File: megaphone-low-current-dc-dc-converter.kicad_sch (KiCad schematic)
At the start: 7 parts, among them U2 AP63203WU

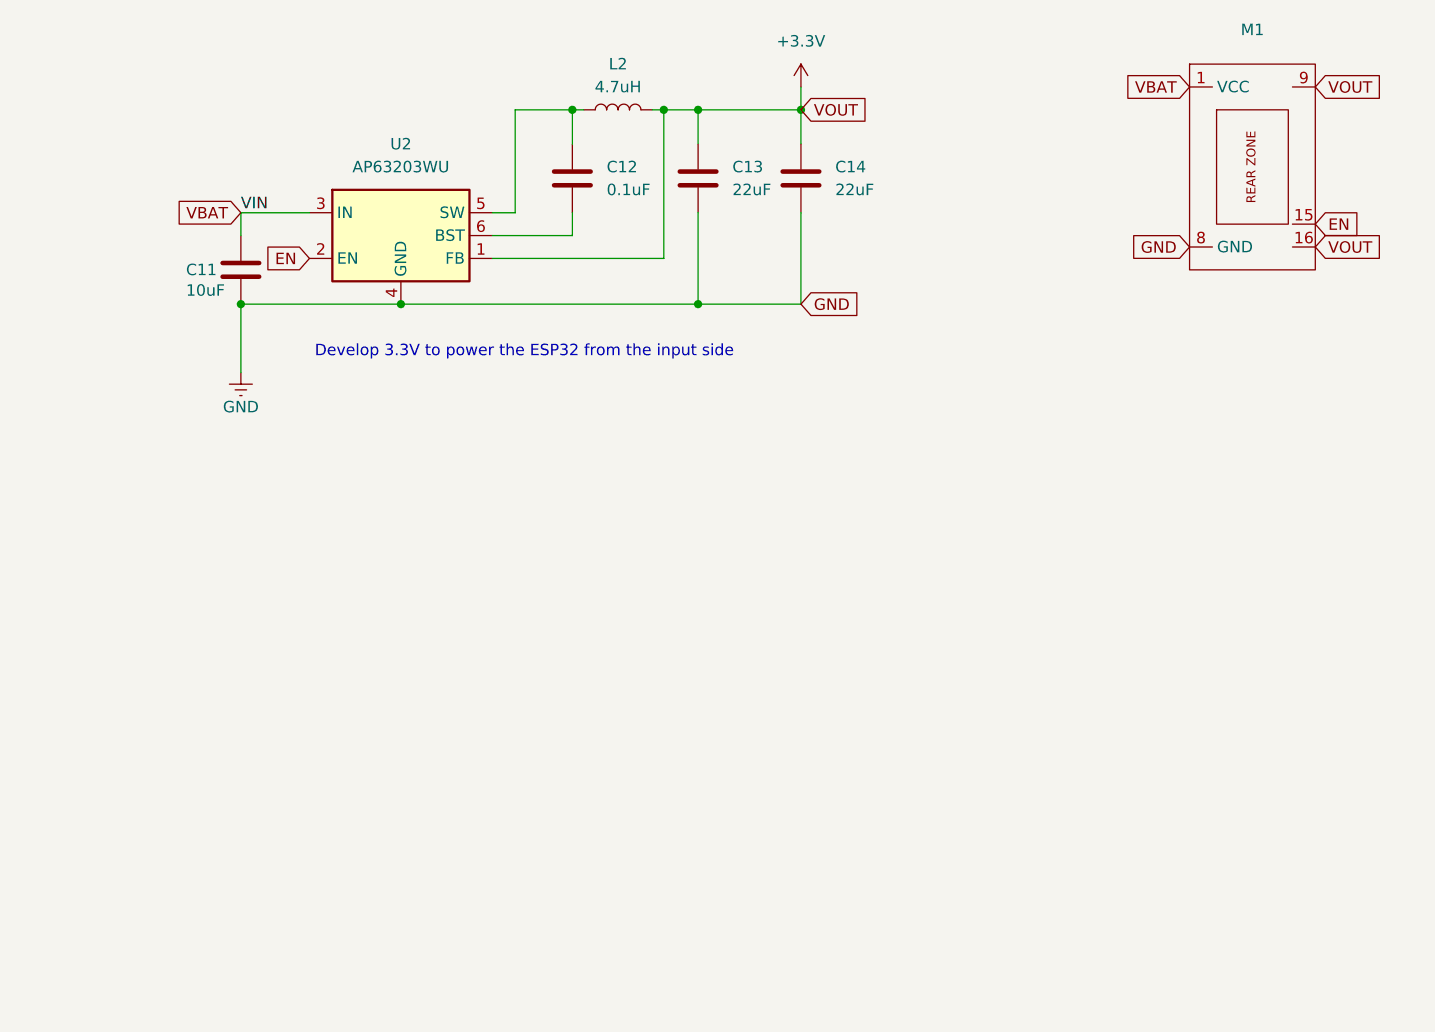
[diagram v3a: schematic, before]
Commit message: use TPS631000 DC:DC converter
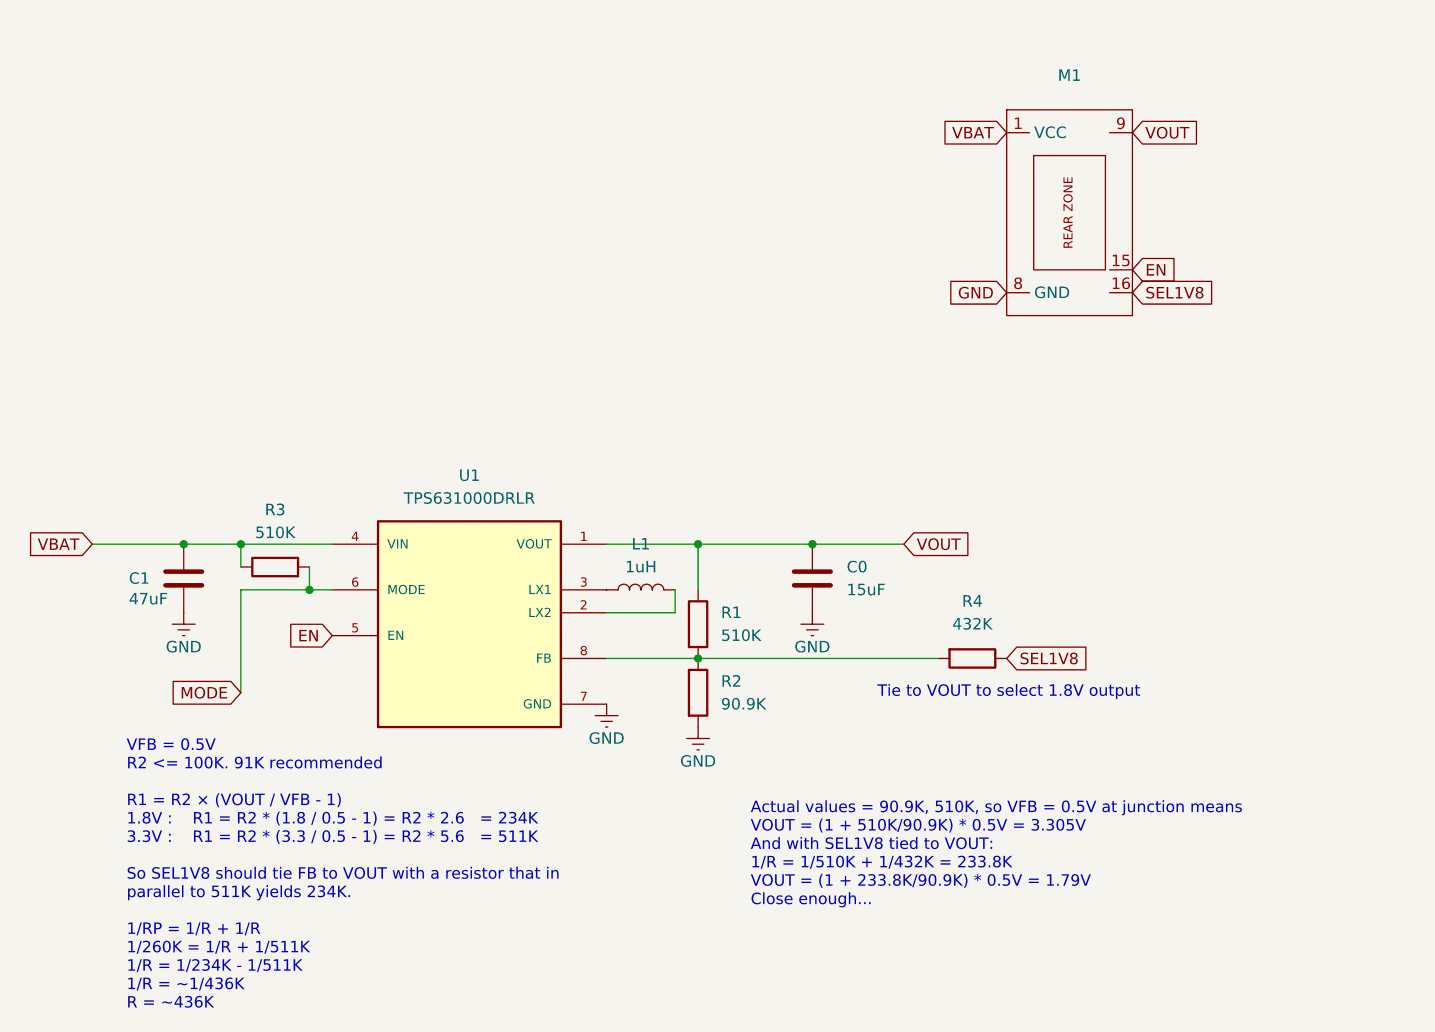
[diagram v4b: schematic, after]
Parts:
- removed C12: 0.1uF, Capacitor_SMD:C_0603_1608Metric, symbol Device:C
- removed C13, C14: 22uF, Capacitor_SMD:C_0603_1608Metric, symbol Device:C
- removed U2: AP63203WU, Package_TO_SOT_SMD:TSOT-23-6, symbol Regulator_Switching:AP63203WU
- added C0: 15uF, Capacitor_SMD:C_0805_2012Metric, symbol Device:C
- added R1, R3: 510K, Resistor_SMD:R_0805_2012Metric, symbol Device:R
- added R2: 90.9K, Resistor_SMD:R_0805_2012Metric, symbol Device:R
- added R4: 432K, Resistor_SMD:R_0805_2012Metric, symbol Device:R
- added U1: TPS631000DRLR, megaphone-low-current-dc-dc-converter:SOT50P160X60-8N, symbol TPS631000DRLR:TPS631000DRLR
- C1: renamed from C11; value 10uF -> 47uF; footprint Capacitor_SMD:C_0603_1608Metric -> Capacitor_SMD:C_0805_2012Metric
- L1: renamed from L2; value 4.7uH -> 1uH; footprint Inductor_SMD:L_Vishay_IFSC-1515AH_4x4x1.8mm -> Inductor_SMD:L_1008_2520Metric_Pad1.43x2.20mm_HandSolder
- M1: footprint MegaCastle:MegaCastle2x8-Module-I7.0x15.5-M8183 -> MegaCastle:MegaCastle2x8-Module-I7.0x15.5-M8183-PANEL-NIBBLE
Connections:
- net EN: now also U1.5 (EN)
- net GND: now also C0.2, R2.2, U1.7 (GND)
- net VBAT: now also R3.1, U1.4 (VIN)
- net at L1.1: now also U1.3 (LX1)
- removed net +3.3V: L1.2, M1.16, M1.9
- new net: R1.2, R2.1, R4.2, U1.8 (FB)
- new net: L1.2, U1.2 (LX2)
- new net MODE: R3.2, U1.6 (MODE)
- new net SEL1V8: M1.16, R4.1
- new net VOUT: C0.1, M1.9, R1.1, U1.1 (VOUT)
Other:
- note added: "Actual values = 90.9K, 510K, so VFB = 0.5V at junction means VOUT = (1 + 510K/90.9K) * 0.5V = 3.305V And with SEL1V8 tied to VOUT: 1/R = 1/510K + 1/432K = 233.8K VOUT = (1 + 233.8K/90.9K) * 0.5V = 1.79V Close enough..."
- note added: "Tie to VOUT to select 1.8V output"
- note added: "VFB = 0.5V R2 <= 100K. 91K recommended R1 = R2 × (VOUT / VFB - 1) 1.8V : R1 = R2 * (1.8 / 0.5 - 1) = R2 * 2.6 = 234K 3.3V : R1 = R2 * (3.3 / 0.5 - 1) = R2 * 5.6 = 511K So SEL1V8 should tie FB to VOUT with a resistor that in parallel to 511K yields 234K. 1/RP = 1/R + 1/R 1/260K = 1/R + 1/511K 1/R = 1/234K - 1/511K 1/R = ~1/436K R = ~436K"
- note removed: "Develop 3.3V to power the ESP32 from the input side"
- moved on the sheet: C1, L1, M1

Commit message: finish PCB layout
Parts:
- removed M1: ~, MegaCastle:MegaCastle2x8-Module-I7.0x15.5-M8183-PANEL-NIBBLE, symbol MegaCastle:MegaCastle2x8-Module-I7.0x15.5-M8183
- added M2: ~, MegaCastle:MegaCastle2x8-Module-I7.0x15.5-M8187-PANEL-NIBBLE, symbol MegaCastle:MegaCastle2x8-Module-I7.0x15.5-M8187
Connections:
- net EN: now also M2.14
- net GND: now also M2.8 (GND)
- net MODE: now also M2.15
- net SEL1V8: now also M2.16
- net VBAT: now also M2.1 (VCC)
- net VOUT: now also M2.9
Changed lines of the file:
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@@
 	(global_label "SEL1V8"
 		(shape input)
-		(at 138.43 63.5 0)
+		(at 92.71 73.66 0)
 		(fields_autoplaced yes)
 		(effects
@@
 		)
 		(property "Intersheetrefs" "${INTERSHEET_REFS}"
-			(at 148.3094 63.5 0)
+			(at 102.5894 73.66 0)
 			(effects
 				(font
@@
 	(global_label "VBAT"
 		(shape input)
-		(at 124.46 45.72 180)
+		(at 78.74 55.88 180)
 		(fields_autoplaced yes)
 		(effects
@@
 		)
 		(property "Intersheetrefs" "${INTERSHEET_REFS}"
-			(at 117.06 45.72 0)
+			(at 71.34 55.88 0)
 			(effects
 				(font
@@
 	(global_label "EN"
 		(shape input)
-		(at 138.43 60.96 0)
+		(at 92.71 68.58 0)
 		(fields_autoplaced yes)
 		(effects
@@
 		)
 		(property "Intersheetrefs" "${INTERSHEET_REFS}"
-			(at 143.8947 60.96 0)
+			(at 98.1747 68.58 0)
 			(effects
 				(font
@@
 	(global_label "VOUT"
 		(shape input)
-		(at 138.43 45.72 0)
+		(at 92.71 55.88 0)
 		(fields_autoplaced yes)
 		(effects
@@
 		)
 		(property "Intersheetrefs" "${INTERSHEET_REFS}"
-			(at 146.1324 45.72 0)
+			(at 100.4124 55.88 0)
 			(effects
 				(font
@@
 	(global_label "GND"
 		(shape input)
-		(at 124.46 63.5 180)
+		(at 78.74 73.66 180)
 		(fields_autoplaced yes)
 		(effects
@@
 		)
 		(property "Intersheetrefs" "${INTERSHEET_REFS}"
-			(at 117.6043 63.5 0)
+			(at 71.8843 73.66 0)
 			(effects
 				(font
@@
 		(property "Intersheetrefs" "${INTERSHEET_REFS}"
 			(at 120.7324 91.44 0)
+			(effects
+				(font
+					(size 1.27 1.27)
+				)
+				(justify left)
+				(hide yes)
+			)
+		)
+	)
+	(global_label "MODE"
+		(shape input)
+		(at 92.71 71.12 0)
+		(fields_autoplaced yes)
+		(effects
+			(font
+				(size 1.27 1.27)
+			)
+			(justify left)
+		)
+		(property "Intersheetrefs" "${INTERSHEET_REFS}"
+			(at 100.8961 71.12 0)
 			(effects
 				(font
@@
 	)
 	(symbol
+		(lib_id "MegaCastle:MegaCastle2x8-Module-I7.0x15.5-M8187")
+		(at 85.09 64.77 0)
+		(unit 1)
+		(exclude_from_sim no)
+		(in_bom yes)
+		(on_board yes)
+		(dnp no)
+		(fields_autoplaced yes)
+		(property "Reference" "M2"
+			(at 85.725 49.53 0)
+			(effects
+				(font
+					(size 1.27 1.27)
+				)
+			)
+		)
+		(property "Value" "~"
+			(at 85.725 52.07 0)
+			(effects
+				(font
+					(size 1.27 1.27)
+				)
+			)
+		)
+		(property "Footprint" "MegaCastle:MegaCastle2x8-Module-I7.0x15.5-M8187-PANEL-NIBBLE"
+			(at 85.09 81.28 0)
+			(effects
+				(font
+					(size 1.27 1.27)
+				)
+				(hide yes)
+			)
+		)
+		(property "Datasheet" ""
+			(at 85.09 59.69 0)
+			(effects
+				(font
+					(size 1.27 1.27)
+				)
+				(hide yes)
+			)
+		)
+		(property "Description" "Generated using footprint-gen .. 7 14 6 M8187"
+			(at 85.09 64.77 0)
+			(effects
+				(font
+					(size 1.27 1.27)
+				)
+				(hide yes)
+			)
+		)
+		(pin "14"
+		)
+		(pin "16"
+		)
+		(pin "8"
+		)
+		(pin "1"
+		)
+		(pin "15"
+		)
+		(pin "9"
+		)
+		(instances
+			(project ""
+				(path "/6fccb5b0-46ff-4014-9169-aa61e4064f3f"
+					(reference "M2")
+					(unit 1)
+				)
+			)
+		)
+	)
+	(symbol
 		(lib_id "power:Earth")
 		(at 80.01 109.22 0)
@@
 					(unit 1)
 				)
-			)
-		)
-	)
-	(symbol
-		(lib_id "MegaCastle:MegaCastle2x8-Module-I7.0x15.5-M8183")
-		(at 130.81 54.61 0)
-		(unit 1)
-		(exclude_from_sim no)
-		(in_bom yes)
-		(on_board yes)
-		(dnp no)
-		(fields_autoplaced yes)
-		(property "Reference" "M1"
-			(at 131.445 39.37 0)
-			(effects
-				(font
-					(size 1.27 1.27)
-				)
-			)
-		)
-		(property "Value" "~"
-			(at 131.445 41.91 0)
-			(effects
-				(font
-					(size 1.27 1.27)
-				)
-			)
-		)
-		(property "Footprint" "MegaCastle:MegaCastle2x8-Module-I7.0x15.5-M8183-PANEL-NIBBLE"
-			(at 130.81 71.12 0)
-			(effects
-				(font
-					(size 1.27 1.27)
-				)
-				(hide yes)
-			)
-		)
-		(property "Datasheet" ""
-			(at 130.81 49.53 0)
-			(effects
-				(font
-					(size 1.27 1.27)
-				)
-				(hide yes)
-			)
-		)
-		(property "Description" "Generated using footprint-gen .. 7 14 5 M8183"
-			(at 130.81 54.61 0)
-			(effects
-				(font
-					(size 1.27 1.27)
-				)
-				(hide yes)
-			)
-		)
-		(pin "1"
-		)
-		(pin "8"
-		)
-		(pin "9"
-		)
-		(pin "16"
-		)
-		(pin "15"
-		)
-		(instances
-			(project ""
-				(path "/6fccb5b0-46ff-4014-9169-aa61e4064f3f"
-					(reference "M1")
-					(unit 1)
-				)

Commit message: Updating footprint, and re-routing
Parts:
- M2: footprint MegaCastle:MegaCastle2x8-Module-I7.0x15.5-M8187-PANEL-NIBBLE -> megaphone-low-current-dc-dc-converter Footprint Library:MegaCastle2x8-Module-I15.0x15.5-M8187-SPAREPAD
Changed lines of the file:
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@@
 (kicad_sch
-	(version 20231120)
+	(version 20250114)
 	(generator "eeschema")
-	(generator_version "8.0")
+	(generator_version "9.0")
 	(paper "A4")
 	(title_block
@@
 		(comment 2 "Adapted for 3.5V output voltage")
 	)
+	(text "VFB = 0.5V\nR2 <= 100K. 91K recommended\n\nR1 = R2 × (VOUT / VFB - 1)\n1.8V :    R1 = R2 * (1.8 / 0.5 - 1) = R2 * 2.6   = 234K\n3.3V :    R1 = R2 * (3.3 / 0.5 - 1) = R2 * 5.6   = 511K\n\nSo SEL1V8 should tie FB to VOUT with a resistor that in\nparallel to 511K yields 234K.\n\n1/RP = 1/R + 1/R\n1/260K = 1/R + 1/511K\n1/R = 1/234K - 1/511K\n1/R = ~1/436K\nR = ~436K"
+		(exclude_from_sim no)
+		(at 26.67 128.27 0)
+		(effects
+			(font
+				(size 1.27 1.27)
+			)
+			(justify left)
+		)
+	)
+	(text "Actual values = 90.9K, 510K, so VFB = 0.5V at junction means\nVOUT = (1 + 510K/90.9K) * 0.5V = 3.305V\nAnd with SEL1V8 tied to VOUT:\n1/R = 1/510K + 1/432K = 233.8K\nVOUT = (1 + 233.8K/90.9K) * 0.5V = 1.79V\nClose enough..."
+		(exclude_from_sim no)
+		(at 96.012 125.984 0)
+		(effects
+			(font
+				(size 1.27 1.27)
+			)
+			(justify left)
+		)
+	)
+	(text "Tie to VOUT to select 1.8V output"
+		(exclude_from_sim no)
+		(at 124.714 107.95 0)
+		(effects
+			(font
+				(size 1.27 1.27)
+			)
+		)
+	)
 	(junction
 		(at 90.17 91.44)
@@
 			(width 0)
 			(type default)
-		)
-	)
-	(text "VFB = 0.5V\nR2 <= 100K. 91K recommended\n\nR1 = R2 × (VOUT / VFB - 1)\n1.8V :    R1 = R2 * (1.8 / 0.5 - 1) = R2 * 2.6   = 234K\n3.3V :    R1 = R2 * (3.3 / 0.5 - 1) = R2 * 5.6   = 511K\n\nSo SEL1V8 should tie FB to VOUT with a resistor that in\nparallel to 511K yields 234K.\n\n1/RP = 1/R + 1/R\n1/260K = 1/R + 1/511K\n1/R = 1/234K - 1/511K\n1/R = ~1/436K\nR = ~436K"
-		(exclude_from_sim no)
-		(at 26.67 128.27 0)
-		(effects
-			(font
-				(size 1.27 1.27)
-			)
-			(justify left)
-		)
-	)
-	(text "Actual values = 90.9K, 510K, so VFB = 0.5V at junction means\nVOUT = (1 + 510K/90.9K) * 0.5V = 3.305V\nAnd with SEL1V8 tied to VOUT:\n1/R = 1/510K + 1/432K = 233.8K\nVOUT = (1 + 233.8K/90.9K) * 0.5V = 1.79V\nClose enough..."
-		(exclude_from_sim no)
-		(at 96.012 125.984 0)
-		(effects
-			(font
-				(size 1.27 1.27)
-			)
-			(justify left)
-		)
-	)
-	(text "Tie to VOUT to select 1.8V output"
-		(exclude_from_sim no)
-		(at 124.714 107.95 0)
-		(effects
-			(font
-				(size 1.27 1.27)
-			)
 		)
 	)
@@
 			)
 		)
-		(property "Footprint" "MegaCastle:MegaCastle2x8-Module-I7.0x15.5-M8187-PANEL-NIBBLE"
+		(property "Footprint" "megaphone-low-current-dc-dc-converter Footprint Library:MegaCastle2x8-Module-I15.0x15.5-M8187-SPAREPAD"
 			(at 85.09 81.28 0)
 			(effects
@@
 		)
 	)
+	(embedded_fonts no)
 )

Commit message: Adding JLCPCB production files
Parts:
- C0: LCSC (none) -> C23692982
- C1: LCSC (none) -> C16780
- L1: LCSC (none) -> C882955
- M2: now not fitted; now left out of the parts list
- R1, R3: LCSC (none) -> C2907332
- R2: LCSC (none) -> C229044
- R4: LCSC (none) -> C137526
- U1: LCSC (none) -> C5219190
